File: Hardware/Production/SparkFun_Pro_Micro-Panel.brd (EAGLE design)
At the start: 104.6 x 128.3 mm, 1563 parts, among them J1 Qwiic, J13 Qwiic, J17 Qwiic, J2 Qwiic, J21 Qwiic, J25 Qwiic, J29 Qwiic, J33 Qwiic, J37 Qwiic, J41 Qwiic, J45 Qwiic, J49 Qwiic, J53 Qwiic, J57 Qwiic, J9 Qwiic, U1 3.3V, U10 3.3V, U11 ATmega32U4, U12 3.3V, U13 ATmega32U4, U14 3.3V, U15 ATmega32U4, U16 3.3V, U17 ATmega32U4, U18 3.3V, U19 ATmega32U4, U2 ATmega32U4, U20 3.3V, U21 ATmega32U4, U22 3.3V, U23 ATmega32U4, U24 3.3V, U25 ATmega32U4, U26 3.3V, U27 ATmega32U4, U28 3.3V, U29 ATmega32U4, U3 ATmega32U4, U30 3.3V, U4 3.3V, U5 ATmega32U4, U6 3.3V, U7 ATmega32U4, U8 3.3V, U9 ATmega32U4, Y1 32MHz, Y10 32MHz, Y11 32MHz, Y12 32MHz, Y13 32MHz, Y14 32MHz, Y15 32MHz, Y2 32MHz, Y3 32MHz, Y4 32MHz, Y5 32MHz, Y6 32MHz, Y7 32MHz, Y8 32MHz, Y9 32MHz

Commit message: Adding production panel, pro micro FP test brd, and castellated test lbr.
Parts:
- U$100, U$164, U$228, U$292, U$356, U$420, U$484, U$548, U$612, U$676, U$740, U$804, U$868, U$932: device buzzard_labels (18):3V39 -> buzzard_labels (15):A29
- U$101, U$165, U$229, U$293, U$357, U$421, U$485, U$549, U$613, U$677, U$741, U$805, U$869, U$933: device buzzard_labels (15):A310 -> buzzard_labels (15):A18
- U$102, U$166, U$230, U$294, U$358, U$422, U$486, U$550, U$614, U$678, U$742, U$806, U$870, U$934: device buzzard_labels (15):A29 -> buzzard_labels (15):A07
- U$103, U$167, U$231, U$295, U$359, U$423, U$487, U$551, U$615, U$679, U$743, U$807, U$871, U$935: device buzzard_labels (15):A18 -> buzzard_labels (15):156
- U$104, U$168, U$232, U$296, U$360, U$424, U$488, U$552, U$616, U$680, U$744, U$808, U$872, U$936: device buzzard_labels (15):A07 -> buzzard_labels (15):145
- U$105, U$169, U$233, U$297, U$361, U$425, U$489, U$553, U$617, U$681, U$745, U$809, U$873, U$937: device buzzard_labels (15):156 -> buzzard_labels (15):164
- U$106, U$170, U$234, U$298, U$362, U$426, U$490, U$554, U$618, U$682, U$746, U$810, U$874, U$938: device buzzard_labels (15):145 -> buzzard_labels (14):104
- U$107, U$171, U$235, U$299, U$363, U$427, U$491, U$555, U$619, U$683, U$747, U$811, U$875, U$939: device buzzard_labels (15):164 -> buzzard_labels (15):911
- U$108, U$172, U$236, U$300, U$364, U$428, U$492, U$556, U$620, U$684, U$748, U$812, U$876, U$940: device buzzard_labels (14):104 -> buzzard_labels (15):812
- U$109, U$173, U$237, U$301, U$365, U$429, U$493, U$557, U$621, U$685, U$749, U$813, U$877, U$941: device buzzard_labels (15):911 -> buzzard_labels (15):713
- U$110, U$174, U$238, U$302, U$366, U$430, U$494, U$558, U$622, U$686, U$750, U$814, U$878, U$942: device buzzard_labels (15):812 -> buzzard_labels (15):614
- U$111, U$175, U$239, U$303, U$367, U$431, U$495, U$559, U$623, U$687, U$751, U$815, U$879, U$943: device buzzard_labels (15):713 -> buzzard_labels (15):515
- U$112, U$176, U$240, U$304, U$368, U$432, U$496, U$560, U$624, U$688, U$752, U$816, U$880, U$944: device buzzard_labels (15):614 -> buzzard_labels (13):45
- U$113, U$177, U$241, U$305, U$369, U$433, U$497, U$561, U$625, U$689, U$753, U$817, U$881, U$945: device buzzard_labels (15):515 -> buzzard_labels (15):317
- U$114, U$178, U$242, U$306, U$370, U$434, U$498, U$562, U$626, U$690, U$754, U$818, U$882, U$946: device buzzard_labels (13):45 -> buzzard_labels (15):218
- U$115, U$179, U$243, U$307, U$371, U$435, U$499, U$563, U$627, U$691, U$755, U$819, U$883, U$947: device buzzard_labels (15):317 -> buzzard_labels (16):GND4
- U$116, U$180, U$244, U$308, U$372, U$436, U$500, U$564, U$628, U$692, U$756, U$820, U$884, U$948: device buzzard_labels (15):218 -> buzzard_labels (15):RX20
- U$117, U$181, U$245, U$309, U$373, U$437, U$501, U$565, U$629, U$693, U$757, U$821, U$885, U$949: device buzzard_labels (16):GND4 -> buzzard_labels (13):TX2
- U$118, U$182, U$246, U$310, U$374, U$438, U$502, U$566, U$630, U$694, U$758, U$822, U$886, U$950: device buzzard_labels (15):RX20 -> buzzard_labels (17):GND4
- U$119, U$183, U$247, U$311, U$375, U$439, U$503, U$567, U$631, U$695, U$759, U$823, U$887, U$951: device buzzard_labels (13):TX2 -> buzzard_labels (18):3V39
- U$120, U$184, U$248, U$312, U$376, U$440, U$504, U$568, U$632, U$696, U$760, U$824, U$888, U$952: device buzzard_labels (17):GND4 -> buzzard_labels (13):G1
- U$121, U$185, U$249, U$313, U$377, U$441, U$505, U$569, U$633, U$697, U$761, U$825, U$889, U$953: device buzzard_labels (18):3V39 -> buzzard_labels (13):V0
- U$122, U$186, U$250, U$314, U$378, U$442, U$506, U$570, U$634, U$698, U$762, U$826, U$890, U$954: device buzzard_labels (13):G1 -> buzzard_labels (14):D#3
- U$123, U$187, U$251, U$315, U$379, U$443, U$507, U$571, U$635, U$699, U$763, U$827, U$891, U$955: device buzzard_labels (13):V0 -> buzzard_labels (14):D#4
- U$124, U$188, U$252, U$316, U$380, U$444, U$508, U$572, U$636, U$700, U$764, U$828, U$892, U$956: device buzzard_labels (14):D#3 -> buzzard_labels (10):PWR0
- U$125, U$189, U$253, U$317, U$381, U$445, U$509, U$573, U$637, U$701, U$765, U$829, U$893, U$957: device buzzard_labels (14):D#4 -> buzzard_labels (10):5V1
- U$126, U$190, U$254, U$318, U$382, U$446, U$510, U$574, U$638, U$702, U$766, U$830, U$894, U$958: device buzzard_labels (10):PWR0 -> buzzard_labels (11):VCC1
- U$128, U$192, U$256, U$320, U$384, U$448, U$512, U$576, U$640, U$704, U$768, U$832, U$896, U$960: device buzzard_labels (11):VCC1 -> buzzard_labels (10):5V1
- U$15: device buzzard_labels (18):3V39 -> buzzard_labels (10):5V1
- U$163, U$227, U$291, U$355, U$419, U$483, U$547, U$611, U$675, U$739, U$803, U$867, U$931, U$99: device buzzard_labels (18):3V39 -> buzzard_labels (15):A310
- U$33: value (none) -> OSHW-LOGOMINI; device buzzard_labels (18):3V39 -> SparkFun-Aesthetics:OSHW-LOGO-MINI
- U$65: value OSHW-LOGOMINI -> (none); device SparkFun-Aesthetics:OSHW-LOGO-MINI -> buzzard_labels (10):5V1
- moved U$33 23.2 mm to (34.5, 31.5), flipped to the bottom, turned to 0 degrees
- moved U$65 22.9 mm to (14.7, 20.1), flipped to the top, turned to 90 degrees
- moved U$940 12.8 mm to (77.1, 74.9)
- moved U$300 12.8 mm to (77.1, 3.81)
- moved U$620 12.8 mm to (77.1, 39.4)
- moved U$684 12.8 mm to (3.94, 74.9)
- moved U$364 12.8 mm to (3.94, 39.4)
- moved U$748 12.8 mm to (22.2, 74.9)
- moved U$812 12.8 mm to (40.5, 74.9)
- moved U$108 12.8 mm to (22.2, 3.81)
- moved U$172 12.8 mm to (40.5, 3.81)
- moved U$428 12.8 mm to (22.2, 39.4)
- moved U$492 12.8 mm to (40.5, 39.4)
- moved U$876 12.8 mm to (58.8, 74.9)
- moved U$236 12.8 mm to (58.8, 3.81)
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
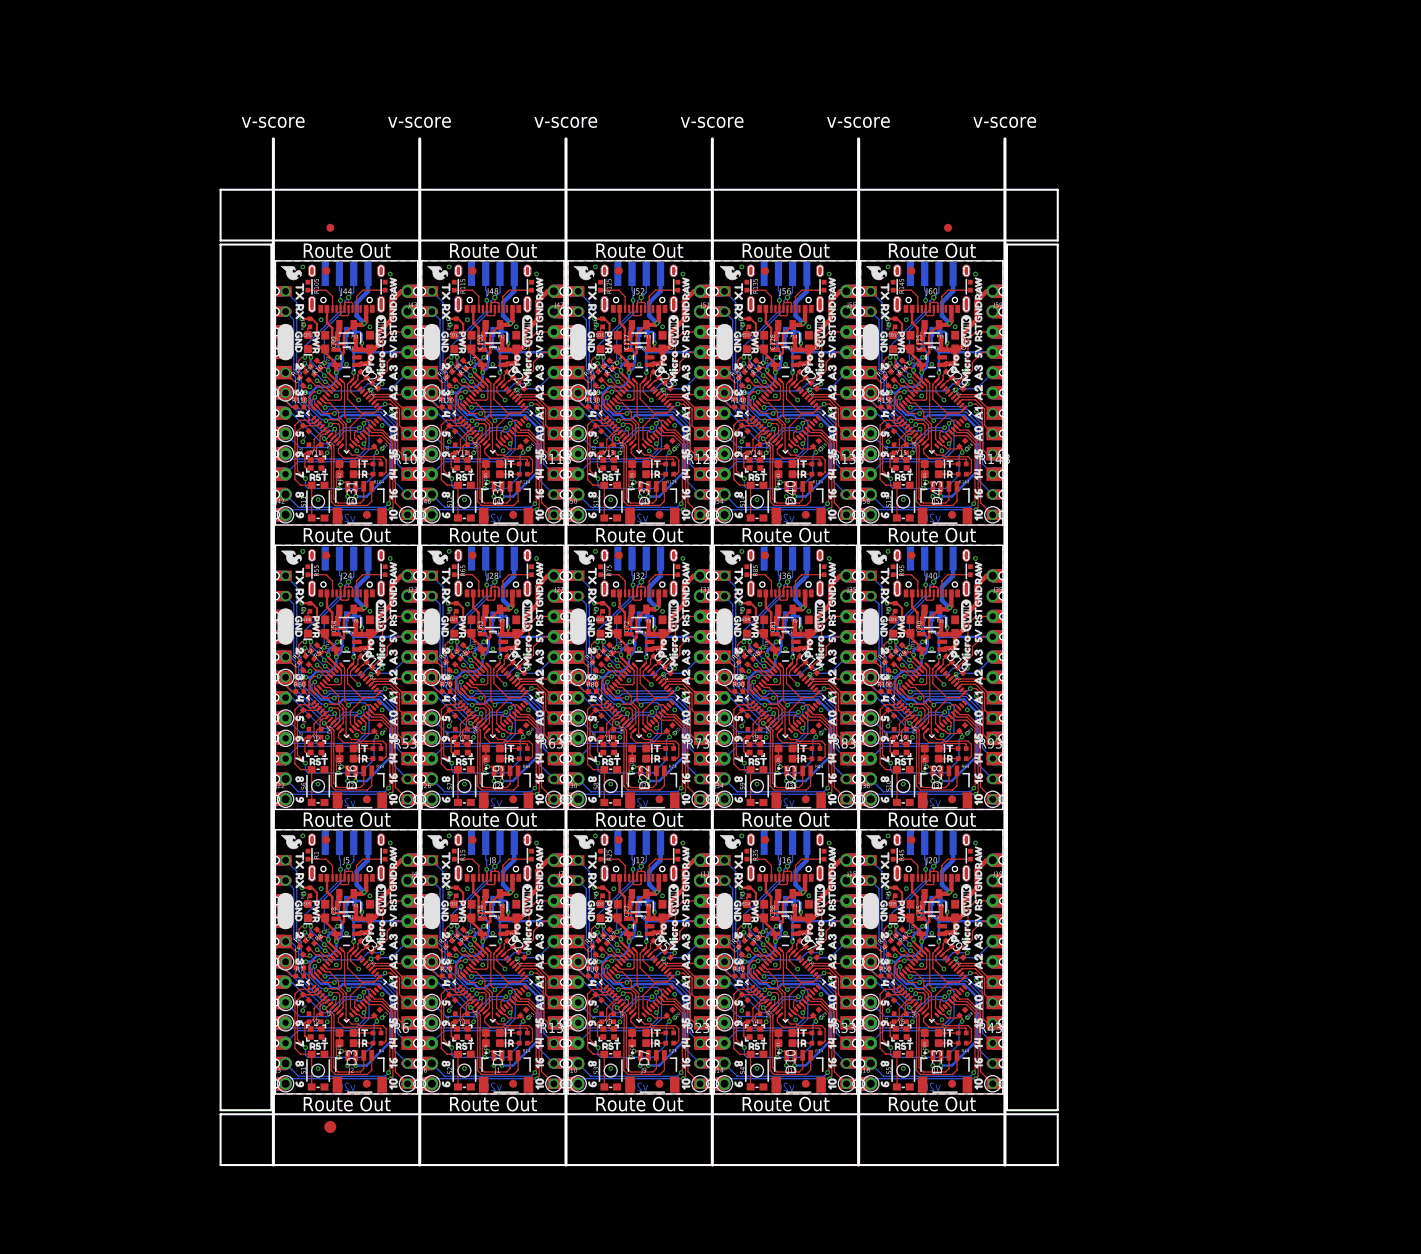
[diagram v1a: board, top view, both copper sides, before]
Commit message: Updates to Pro Micro and Frank
"Castellated" library '1x12CASTELLATED' and 'PRO_MICRO_C' footprints updated and 'PRO_MICRO_C' device updated.

Pro Micro C got uniform drill/ring sizing + added plated holes to outside in place of drills

Frank got 1U Keycap standard switch spacing and updated Pro Micro footprint.
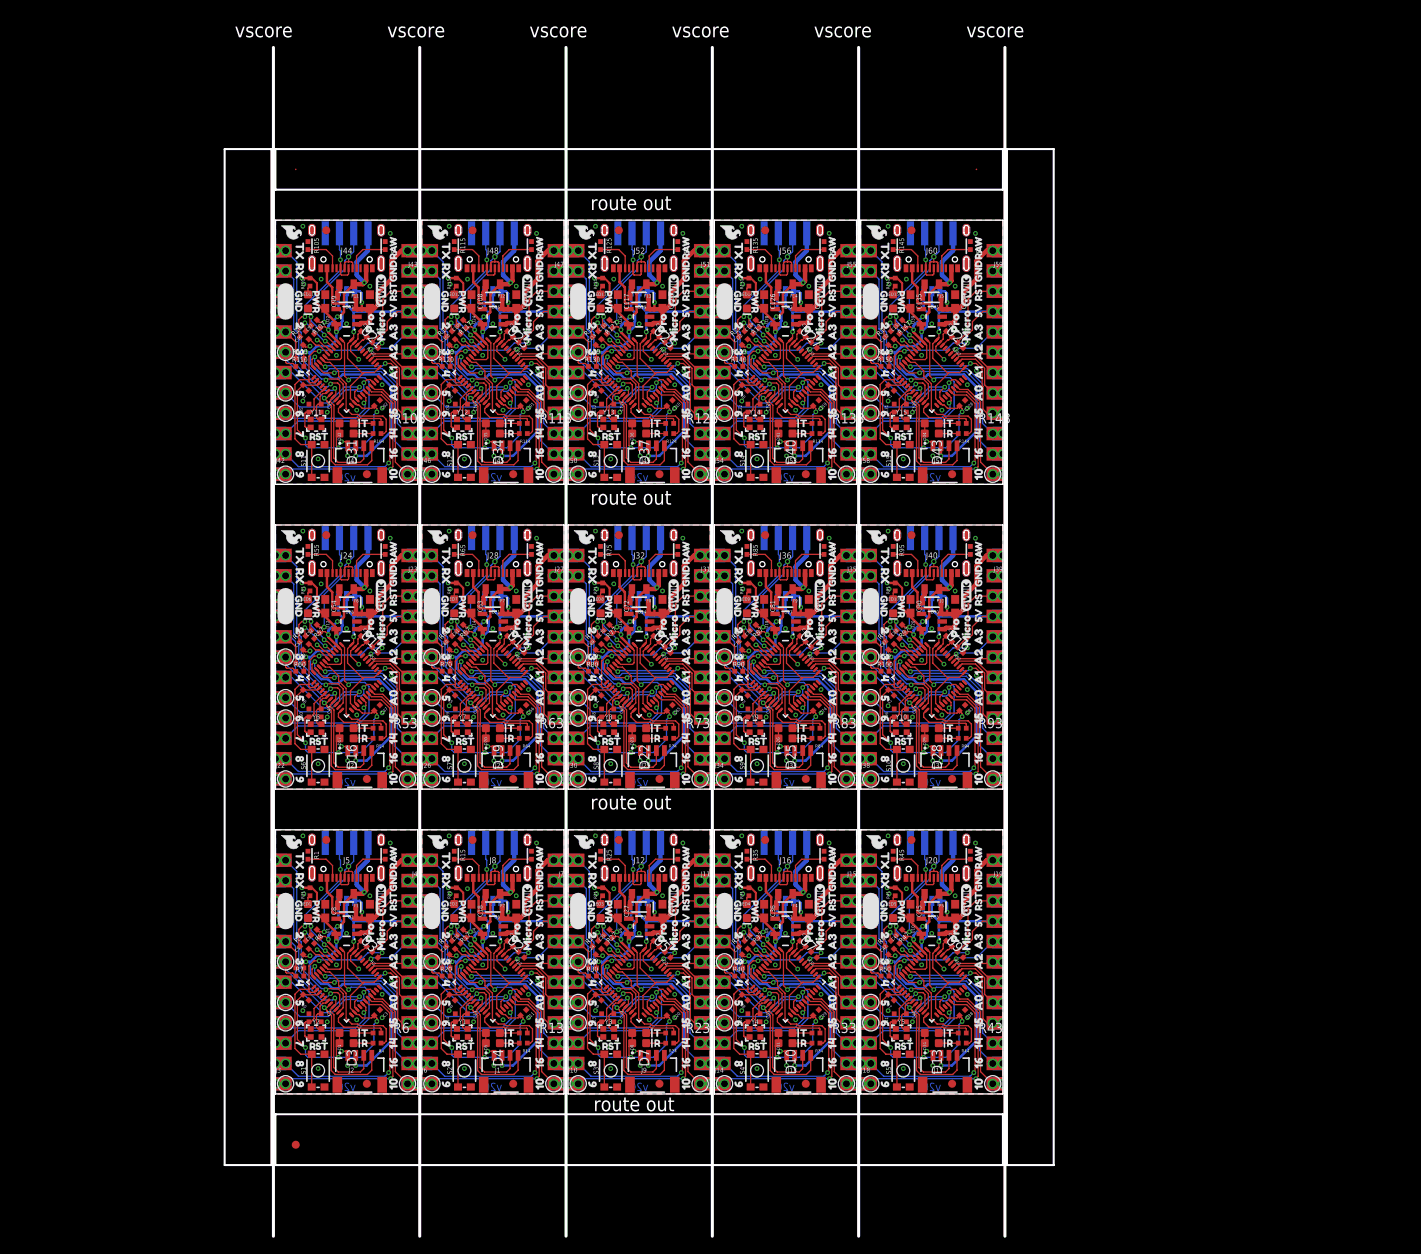
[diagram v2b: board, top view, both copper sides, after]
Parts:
- removed U$946: (no value), buzzard_labels (15):218
- removed U$947: (no value), buzzard_labels (16):GND4
- removed U$948: (no value), buzzard_labels (15):RX20
- removed U$949: (no value), buzzard_labels (13):TX2
- removed U$950: (no value), buzzard_labels (17):GND4
- removed U$951: (no value), buzzard_labels (18):3V39
- removed U$952: (no value), buzzard_labels (13):G1
- removed U$953: (no value), buzzard_labels (13):V0
- removed U$954: (no value), buzzard_labels (14):D#3
- removed U$955: (no value), buzzard_labels (14):D#4
- removed U$956: (no value), buzzard_labels (10):PWR0
- removed U$957, U$959, U$960: (no value), buzzard_labels (10):5V1
- removed U$958: (no value), buzzard_labels (11):VCC1
- E$2: device SparkFun-Aesthetics:FIDUCIAL-1X2 -> SparkFun-Aesthetics:FIDUCIAL-0.2MM
- E$3: device SparkFun-Retired:FIDUCIAL-1.5X3 -> SparkFun-Aesthetics:FIDUCIAL-0.2MM
- U$100: device buzzard_labels (15):A29 -> buzzard_labels (15):A07
- U$101: device buzzard_labels (15):A18 -> buzzard_labels (15):156
- U$102, U$401: device buzzard_labels (15):A07 -> buzzard_labels (15):145
- U$103: device buzzard_labels (15):156 -> buzzard_labels (15):164
- U$104: device buzzard_labels (15):145 -> buzzard_labels (14):104
- U$105, U$393: device buzzard_labels (15):164 -> buzzard_labels (15):911
- U$106, U$581: device buzzard_labels (14):104 -> buzzard_labels (15):812
- U$107: device buzzard_labels (15):911 -> buzzard_labels (15):713
- U$108: device buzzard_labels (15):812 -> buzzard_labels (15):614
- U$109: device buzzard_labels (15):713 -> buzzard_labels (15):515
- U$110: device buzzard_labels (15):614 -> buzzard_labels (13):45
- U$111: device buzzard_labels (15):515 -> buzzard_labels (15):317
- U$112, U$450: device buzzard_labels (13):45 -> buzzard_labels (15):218
- U$113, U$651: device buzzard_labels (15):317 -> buzzard_labels (16):GND4
- U$114, U$650: device buzzard_labels (15):218 -> buzzard_labels (15):RX20
- U$115: device buzzard_labels (16):GND4 -> buzzard_labels (13):TX2
- U$116, U$469: device buzzard_labels (15):RX20 -> buzzard_labels (17):GND4
- U$117: device buzzard_labels (13):TX2 -> buzzard_labels (18):3V39
- U$118: device buzzard_labels (17):GND4 -> buzzard_labels (13):G1
- U$119: device buzzard_labels (18):3V39 -> buzzard_labels (13):V0
- U$120: device buzzard_labels (13):G1 -> buzzard_labels (14):D#3
- U$121: device buzzard_labels (13):V0 -> buzzard_labels (14):D#4
- U$122: device buzzard_labels (14):D#3 -> buzzard_labels (10):PWR0
- U$123, U$251, U$315: device buzzard_labels (14):D#4 -> buzzard_labels (10):5V1
- U$124: device buzzard_labels (10):PWR0 -> buzzard_labels (11):VCC1
- U$126: device buzzard_labels (11):VCC1 -> buzzard_labels (10):5V1
- U$127, U$253: value (none) -> OSHW-LOGOMINI; device buzzard_labels (10):5V1 -> SparkFun-Aesthetics:OSHW-LOGO-MINI
- U$128, U$191, U$317: device buzzard_labels (10):5V1 -> buzzard_labels (13):45
- U$129: value OSHW-LOGOMINI -> (none); device SparkFun-Aesthetics:OSHW-LOGO-MINI -> buzzard_labels (13):TX2
- U$130: device buzzard_labels (13):45 -> buzzard_labels (14):104
- U$131: device buzzard_labels (13):TX2 -> buzzard_labels (14):MICRO1
- U$132: device SparkFun-Aesthetics:PRODUCTION_INSTRUCTIONS -> buzzard_labels (14):PRO0
- U$133: device buzzard_labels (14):104 -> buzzard_labels (15):156
- U$134: device buzzard_labels (14):MICRO1 -> buzzard_labels (15):164
- U$135: device buzzard_labels (14):PRO0 -> buzzard_labels (15):218
- U$136, U$615: device buzzard_labels (15):156 -> buzzard_labels (15):317
- U$137, U$361: device buzzard_labels (15):164 -> buzzard_labels (15):515
- U$138: device buzzard_labels (15):218 -> buzzard_labels (15):614
- U$139: device buzzard_labels (15):317 -> buzzard_labels (15):713
- U$140: device buzzard_labels (15):515 -> buzzard_labels (15):812
- U$141: device buzzard_labels (15):614 -> buzzard_labels (15):911
- U$142: device buzzard_labels (15):713 -> buzzard_labels (15):A07
- U$143: device buzzard_labels (15):812 -> buzzard_labels (15):A18
- U$144: device buzzard_labels (15):911 -> buzzard_labels (15):A29
- U$145: device buzzard_labels (15):A07 -> buzzard_labels (15):A310
- U$146, U$933: device buzzard_labels (15):A18 -> buzzard_labels (15):RX20
- U$147, U$932: device buzzard_labels (15):A29 -> buzzard_labels (16):GND4
- U$148: device buzzard_labels (15):A310 -> buzzard_labels (16):RST3
- U$149: device buzzard_labels (15):RX20 -> buzzard_labels (15):145
- U$150: device buzzard_labels (16):GND4 -> buzzard_labels (17):R9
- U$151, U$599: device buzzard_labels (16):RST3 -> buzzard_labels (17):RAW5
- U$152: device buzzard_labels (15):145 -> buzzard_labels (17):T8
- U$153, U$537: device buzzard_labels (17):R9 -> buzzard_labels (17):RST3
- U$154: device buzzard_labels (17):RAW5 -> buzzard_labels (17):GND4
- U$155: device buzzard_labels (17):T8 -> buzzard_labels (18):C5
- U$156: device buzzard_labels (17):RST3 -> buzzard_labels (18):MICRO4
- U$157: device buzzard_labels (17):GND4 -> buzzard_labels (18):PRO3
- U$158: device buzzard_labels (18):C5 -> buzzard_labels (17):RAW5
- U$159: device buzzard_labels (18):MICRO4 -> buzzard_labels (17):RST3
- U$160: device buzzard_labels (18):PRO3 -> buzzard_labels (15):A310
- U$161, U$602: device buzzard_labels (17):RAW5 -> buzzard_labels (15):A29
- U$162, U$540: device buzzard_labels (17):RST3 -> buzzard_labels (15):A18
- U$163: device buzzard_labels (15):A310 -> buzzard_labels (15):A07
- U$164: device buzzard_labels (15):A29 -> buzzard_labels (15):156
- U$165, U$338: device buzzard_labels (15):A18 -> buzzard_labels (15):145
- U$166: device buzzard_labels (15):A07 -> buzzard_labels (15):164
- U$167: device buzzard_labels (15):156 -> buzzard_labels (14):104
- U$168: device buzzard_labels (15):145 -> buzzard_labels (15):911
- U$169, U$329: device buzzard_labels (15):164 -> buzzard_labels (15):812
- U$170, U$517: device buzzard_labels (14):104 -> buzzard_labels (15):713
- U$171: device buzzard_labels (15):911 -> buzzard_labels (15):614
- U$172: device buzzard_labels (15):812 -> buzzard_labels (15):515
- U$173: device buzzard_labels (15):713 -> buzzard_labels (13):45
- U$174: device buzzard_labels (15):614 -> buzzard_labels (15):317
- U$175: device buzzard_labels (15):515 -> buzzard_labels (15):218
- U$176: device buzzard_labels (13):45 -> buzzard_labels (16):GND4
- U$177, U$587: device buzzard_labels (15):317 -> buzzard_labels (15):RX20
- U$178: device buzzard_labels (15):218 -> buzzard_labels (13):TX2
- U$179, U$406: device buzzard_labels (16):GND4 -> buzzard_labels (17):GND4
- U$180: device buzzard_labels (15):RX20 -> buzzard_labels (18):3V39
- U$181: device buzzard_labels (13):TX2 -> buzzard_labels (13):G1
- U$182: device buzzard_labels (17):GND4 -> buzzard_labels (13):V0
- U$183: device buzzard_labels (18):3V39 -> buzzard_labels (14):D#3
- U$184: device buzzard_labels (13):G1 -> buzzard_labels (14):D#4
- U$185: device buzzard_labels (13):V0 -> buzzard_labels (10):PWR0
- U$186, U$314, U$378: device buzzard_labels (14):D#3 -> buzzard_labels (10):5V1
- U$187: device buzzard_labels (14):D#4 -> buzzard_labels (11):VCC1
- U$188, U$252: device buzzard_labels (10):PWR0 -> buzzard_labels (10):5V1
- U$190: value (none) -> OSHW-LOGOMINI; device buzzard_labels (11):VCC1 -> SparkFun-Aesthetics:OSHW-LOGO-MINI
- U$192, U$255, U$381: device buzzard_labels (10):5V1 -> buzzard_labels (13):TX2
- U$193: value OSHW-LOGOMINI -> (none); device SparkFun-Aesthetics:OSHW-LOGO-MINI -> buzzard_labels (14):104
- U$194: device buzzard_labels (13):45 -> buzzard_labels (14):MICRO1
- U$195: device buzzard_labels (13):TX2 -> buzzard_labels (14):PRO0
- U$196: device SparkFun-Aesthetics:PRODUCTION_INSTRUCTIONS -> buzzard_labels (15):156
- U$197: device buzzard_labels (14):104 -> buzzard_labels (15):164
- U$198: device buzzard_labels (14):MICRO1 -> buzzard_labels (15):218
- U$199: device buzzard_labels (14):PRO0 -> buzzard_labels (15):317
- U$20: value (none) -> OSHW-LOGOMINI; device SparkFun-Aesthetics:PRODUCTION_INSTRUCTIONS -> SparkFun-Aesthetics:OSHW-LOGO-MINI
- U$200, U$487: device buzzard_labels (15):156 -> buzzard_labels (15):515
- U$201, U$297: device buzzard_labels (15):164 -> buzzard_labels (15):614
- U$202: device buzzard_labels (15):218 -> buzzard_labels (15):713
- U$203: device buzzard_labels (15):317 -> buzzard_labels (15):812
- U$204: device buzzard_labels (15):515 -> buzzard_labels (15):911
- U$205: device buzzard_labels (15):614 -> buzzard_labels (15):A07
- U$206: device buzzard_labels (15):713 -> buzzard_labels (15):A18
- U$207: device buzzard_labels (15):812 -> buzzard_labels (15):A29
- U$208: device buzzard_labels (15):911 -> buzzard_labels (15):A310
- U$209, U$870: device buzzard_labels (15):A07 -> buzzard_labels (15):RX20
- U$210, U$869: device buzzard_labels (15):A18 -> buzzard_labels (16):GND4
- U$211: device buzzard_labels (15):A29 -> buzzard_labels (16):RST3
- U$212, U$291: device buzzard_labels (15):A310 -> buzzard_labels (15):145
- U$213: device buzzard_labels (15):RX20 -> buzzard_labels (17):R9
- U$214, U$662: device buzzard_labels (16):GND4 -> buzzard_labels (17):RAW5
- U$215: device buzzard_labels (16):RST3 -> buzzard_labels (17):T8
- U$216, U$600: device buzzard_labels (15):145 -> buzzard_labels (17):RST3
- U$217: device buzzard_labels (17):R9 -> buzzard_labels (17):GND4
- U$218: device buzzard_labels (17):RAW5 -> buzzard_labels (18):C5
- U$219: device buzzard_labels (17):T8 -> buzzard_labels (18):MICRO4
- U$220: device buzzard_labels (17):RST3 -> buzzard_labels (18):PRO3
- U$221: device buzzard_labels (17):GND4 -> buzzard_labels (17):RAW5
- U$222: device buzzard_labels (18):C5 -> buzzard_labels (17):RST3
- U$223: device buzzard_labels (18):MICRO4 -> buzzard_labels (15):A310
- U$224: device buzzard_labels (18):PRO3 -> buzzard_labels (15):A29
- U$225, U$666: device buzzard_labels (17):RAW5 -> buzzard_labels (15):A18
- U$226, U$604: device buzzard_labels (17):RST3 -> buzzard_labels (15):A07
- U$227: device buzzard_labels (15):A310 -> buzzard_labels (15):156
- U$228, U$275: device buzzard_labels (15):A29 -> buzzard_labels (15):145
- U$229: device buzzard_labels (15):A18 -> buzzard_labels (15):164
- U$230: device buzzard_labels (15):A07 -> buzzard_labels (14):104
- U$231, U$456: device buzzard_labels (15):156 -> buzzard_labels (15):911
- U$232: device buzzard_labels (15):145 -> buzzard_labels (15):812
- U$233, U$265: device buzzard_labels (15):164 -> buzzard_labels (15):713
- U$234, U$453: device buzzard_labels (14):104 -> buzzard_labels (15):614
- U$235: device buzzard_labels (15):911 -> buzzard_labels (15):515
- U$236: device buzzard_labels (15):812 -> buzzard_labels (13):45
- U$237: device buzzard_labels (15):713 -> buzzard_labels (15):317
- U$238: device buzzard_labels (15):614 -> buzzard_labels (15):218
- U$239, U$588: device buzzard_labels (15):515 -> buzzard_labels (16):GND4
- U$240: device buzzard_labels (13):45 -> buzzard_labels (15):RX20
- U$241: device buzzard_labels (15):317 -> buzzard_labels (13):TX2
- U$242: device buzzard_labels (15):218 -> buzzard_labels (17):GND4
- U$243: device buzzard_labels (16):GND4 -> buzzard_labels (18):3V39
- U$244: device buzzard_labels (15):RX20 -> buzzard_labels (13):G1
- U$245: device buzzard_labels (13):TX2 -> buzzard_labels (13):V0
- U$246: device buzzard_labels (17):GND4 -> buzzard_labels (14):D#3
- U$247: device buzzard_labels (18):3V39 -> buzzard_labels (14):D#4
- U$248: device buzzard_labels (13):G1 -> buzzard_labels (10):PWR0
- U$249, U$377, U$441: device buzzard_labels (13):V0 -> buzzard_labels (10):5V1
- U$250: device buzzard_labels (14):D#3 -> buzzard_labels (11):VCC1
- U$254: device buzzard_labels (11):VCC1 -> buzzard_labels (13):45
- U$256, U$319, U$445: device buzzard_labels (10):5V1 -> buzzard_labels (14):104
- U$257: value OSHW-LOGOMINI -> (none); device SparkFun-Aesthetics:OSHW-LOGO-MINI -> buzzard_labels (14):MICRO1
- U$258: device buzzard_labels (13):45 -> buzzard_labels (14):PRO0
- U$259: device buzzard_labels (13):TX2 -> buzzard_labels (15):156
- U$260: device SparkFun-Aesthetics:PRODUCTION_INSTRUCTIONS -> buzzard_labels (15):164
- U$261, U$490: device buzzard_labels (14):104 -> buzzard_labels (15):218
- U$262: device buzzard_labels (14):MICRO1 -> buzzard_labels (15):317
- U$263: device buzzard_labels (14):PRO0 -> buzzard_labels (15):515
- U$264, U$423: device buzzard_labels (15):156 -> buzzard_labels (15):614
- U$266: device buzzard_labels (15):218 -> buzzard_labels (15):812
- U$267: device buzzard_labels (15):317 -> buzzard_labels (15):911
- U$268: device buzzard_labels (15):515 -> buzzard_labels (15):A07
- U$269: device buzzard_labels (15):614 -> buzzard_labels (15):A18
- U$270: device buzzard_labels (15):713 -> buzzard_labels (15):A29
- U$271: device buzzard_labels (15):812 -> buzzard_labels (15):A310
- U$272, U$555: device buzzard_labels (15):911 -> buzzard_labels (15):RX20
- U$273, U$806: device buzzard_labels (15):A07 -> buzzard_labels (16):GND4
- U$274: device buzzard_labels (15):A18 -> buzzard_labels (16):RST3
- U$276: device buzzard_labels (15):A310 -> buzzard_labels (17):R9
- U$277, U$725: device buzzard_labels (15):RX20 -> buzzard_labels (17):RAW5
- U$278: device buzzard_labels (16):GND4 -> buzzard_labels (17):T8
- U$279, U$663: device buzzard_labels (16):RST3 -> buzzard_labels (17):RST3
- U$280, U$872: device buzzard_labels (15):145 -> buzzard_labels (17):GND4
- U$281: device buzzard_labels (17):R9 -> buzzard_labels (18):C5
- U$282: device buzzard_labels (17):RAW5 -> buzzard_labels (18):MICRO4
- U$283: device buzzard_labels (17):T8 -> buzzard_labels (18):PRO3
- U$284: device buzzard_labels (17):RST3 -> buzzard_labels (17):RAW5
- U$285: device buzzard_labels (17):GND4 -> buzzard_labels (17):RST3
- U$286: device buzzard_labels (18):C5 -> buzzard_labels (15):A310
- U$287: device buzzard_labels (18):MICRO4 -> buzzard_labels (15):A29
- U$288: device buzzard_labels (18):PRO3 -> buzzard_labels (15):A18
- U$289, U$730: device buzzard_labels (17):RAW5 -> buzzard_labels (15):A07
- U$290, U$668: device buzzard_labels (17):RST3 -> buzzard_labels (15):156
- U$292: device buzzard_labels (15):A29 -> buzzard_labels (15):164
- U$293: device buzzard_labels (15):A18 -> buzzard_labels (14):104
- U$294: device buzzard_labels (15):A07 -> buzzard_labels (15):911
- U$295, U$392: device buzzard_labels (15):156 -> buzzard_labels (15):812
- U$296: device buzzard_labels (15):145 -> buzzard_labels (15):713
- U$298, U$389: device buzzard_labels (14):104 -> buzzard_labels (15):515
- U$299: device buzzard_labels (15):911 -> buzzard_labels (13):45
- U$300: device buzzard_labels (15):812 -> buzzard_labels (15):317
- U$301: device buzzard_labels (15):713 -> buzzard_labels (15):218
- U$302, U$525: device buzzard_labels (15):614 -> buzzard_labels (16):GND4
- U$303, U$524: device buzzard_labels (15):515 -> buzzard_labels (15):RX20
- U$304, U$66: device buzzard_labels (13):45 -> buzzard_labels (13):TX2
- U$305: device buzzard_labels (15):317 -> buzzard_labels (17):GND4
- U$306: device buzzard_labels (15):218 -> buzzard_labels (18):3V39
- U$307: device buzzard_labels (16):GND4 -> buzzard_labels (13):G1
- U$308: device buzzard_labels (15):RX20 -> buzzard_labels (13):V0
- U$309: device buzzard_labels (13):TX2 -> buzzard_labels (14):D#3
- U$310: device buzzard_labels (17):GND4 -> buzzard_labels (14):D#4
- U$311: device buzzard_labels (18):3V39 -> buzzard_labels (10):PWR0
- U$312, U$440, U$504: device buzzard_labels (13):G1 -> buzzard_labels (10):5V1
- U$313: device buzzard_labels (13):V0 -> buzzard_labels (11):VCC1
- U$316: value (none) -> OSHW-LOGOMINI; device buzzard_labels (10):PWR0 -> SparkFun-Aesthetics:OSHW-LOGO-MINI
- U$318: device buzzard_labels (11):VCC1 -> buzzard_labels (13):TX2
- U$320, U$383, U$509: device buzzard_labels (10):5V1 -> buzzard_labels (14):MICRO1
- U$321: value OSHW-LOGOMINI -> (none); device SparkFun-Aesthetics:OSHW-LOGO-MINI -> buzzard_labels (14):PRO0
- U$322: device buzzard_labels (13):45 -> buzzard_labels (15):156
- U$323: device buzzard_labels (13):TX2 -> buzzard_labels (15):164
- U$324: device SparkFun-Aesthetics:PRODUCTION_INSTRUCTIONS -> buzzard_labels (15):218
- U$325, U$426: device buzzard_labels (14):104 -> buzzard_labels (15):317
- U$326: device buzzard_labels (14):MICRO1 -> buzzard_labels (15):515
- U$327: device buzzard_labels (14):PRO0 -> buzzard_labels (15):614
- U$328, U$359: device buzzard_labels (15):156 -> buzzard_labels (15):713
- U$33: value OSHW-LOGOMINI -> (none); device SparkFun-Aesthetics:OSHW-LOGO-MINI -> buzzard_labels (13):45
- U$330: device buzzard_labels (15):218 -> buzzard_labels (15):911
- U$331: device buzzard_labels (15):317 -> buzzard_labels (15):A07
- U$332: device buzzard_labels (15):515 -> buzzard_labels (15):A18
- U$333: device buzzard_labels (15):614 -> buzzard_labels (15):A29
- U$334: device buzzard_labels (15):713 -> buzzard_labels (15):A310
- U$335, U$492: device buzzard_labels (15):812 -> buzzard_labels (15):RX20
- U$336, U$491: device buzzard_labels (15):911 -> buzzard_labels (16):GND4
- U$337: device buzzard_labels (15):A07 -> buzzard_labels (16):RST3
- U$339: device buzzard_labels (15):A29 -> buzzard_labels (17):R9
- U$340, U$788: device buzzard_labels (15):A310 -> buzzard_labels (17):RAW5
- U$341: device buzzard_labels (15):RX20 -> buzzard_labels (17):T8
- U$342, U$726: device buzzard_labels (16):GND4 -> buzzard_labels (17):RST3
- U$343: device buzzard_labels (16):RST3 -> buzzard_labels (17):GND4
- U$344: device buzzard_labels (15):145 -> buzzard_labels (18):C5
- U$345: device buzzard_labels (17):R9 -> buzzard_labels (18):MICRO4
- U$346: device buzzard_labels (17):RAW5 -> buzzard_labels (18):PRO3
- U$347: device buzzard_labels (17):T8 -> buzzard_labels (17):RAW5
- U$349: device buzzard_labels (17):GND4 -> buzzard_labels (15):A310
- U$350: device buzzard_labels (18):C5 -> buzzard_labels (15):A29
- U$351: device buzzard_labels (18):MICRO4 -> buzzard_labels (15):A18
- U$352: device buzzard_labels (18):PRO3 -> buzzard_labels (15):A07
- U$353, U$794: device buzzard_labels (17):RAW5 -> buzzard_labels (15):156
- U$354, U$732: device buzzard_labels (17):RST3 -> buzzard_labels (15):145
- U$355: device buzzard_labels (15):A310 -> buzzard_labels (15):164
- U$356: device buzzard_labels (15):A29 -> buzzard_labels (14):104
- U$357: device buzzard_labels (15):A18 -> buzzard_labels (15):911
- U$358: device buzzard_labels (15):A07 -> buzzard_labels (15):812
- U$360: device buzzard_labels (15):145 -> buzzard_labels (15):614
- U$362: device buzzard_labels (14):104 -> buzzard_labels (13):45
- U$363: device buzzard_labels (15):911 -> buzzard_labels (15):317
- U$364: device buzzard_labels (15):812 -> buzzard_labels (15):218
- U$365, U$462: device buzzard_labels (15):713 -> buzzard_labels (16):GND4
- U$366, U$461: device buzzard_labels (15):614 -> buzzard_labels (15):RX20
- U$367: device buzzard_labels (15):515 -> buzzard_labels (13):TX2
- U$368: device buzzard_labels (13):45 -> buzzard_labels (17):GND4
- U$369: device buzzard_labels (15):317 -> buzzard_labels (18):3V39
- U$370: device buzzard_labels (15):218 -> buzzard_labels (13):G1
- U$371: device buzzard_labels (16):GND4 -> buzzard_labels (13):V0
- U$372: device buzzard_labels (15):RX20 -> buzzard_labels (14):D#3
- U$373: device buzzard_labels (13):TX2 -> buzzard_labels (14):D#4
- U$374: device buzzard_labels (17):GND4 -> buzzard_labels (10):PWR0
- U$375, U$503, U$567: device buzzard_labels (18):3V39 -> buzzard_labels (10):5V1
- U$376: device buzzard_labels (13):G1 -> buzzard_labels (11):VCC1
- U$379: value (none) -> OSHW-LOGOMINI; device buzzard_labels (14):D#4 -> SparkFun-Aesthetics:OSHW-LOGO-MINI
- U$380: device buzzard_labels (10):PWR0 -> buzzard_labels (13):45
- U$382: device buzzard_labels (11):VCC1 -> buzzard_labels (14):104
- U$384, U$447, U$573: device buzzard_labels (10):5V1 -> buzzard_labels (14):PRO0
- U$385: value OSHW-LOGOMINI -> (none); device SparkFun-Aesthetics:OSHW-LOGO-MINI -> buzzard_labels (15):156
- U$386: device buzzard_labels (13):45 -> buzzard_labels (15):164
- U$387: device buzzard_labels (13):TX2 -> buzzard_labels (15):218
- U$388: device SparkFun-Aesthetics:PRODUCTION_INSTRUCTIONS -> buzzard_labels (15):317
- U$390: device buzzard_labels (14):MICRO1 -> buzzard_labels (15):614
- U$391: device buzzard_labels (14):PRO0 -> buzzard_labels (15):713
- U$394: device buzzard_labels (15):218 -> buzzard_labels (15):A07
- U$395: device buzzard_labels (15):317 -> buzzard_labels (15):A18
- U$396: device buzzard_labels (15):515 -> buzzard_labels (15):A29
- U$397: device buzzard_labels (15):614 -> buzzard_labels (15):A310
- U$398, U$429: device buzzard_labels (15):713 -> buzzard_labels (15):RX20
- U$399, U$428: device buzzard_labels (15):812 -> buzzard_labels (16):GND4
- U$400: device buzzard_labels (15):911 -> buzzard_labels (16):RST3
- U$402: device buzzard_labels (15):A18 -> buzzard_labels (17):R9
- U$403, U$851: device buzzard_labels (15):A29 -> buzzard_labels (17):RAW5
- U$404: device buzzard_labels (15):A310 -> buzzard_labels (17):T8
- U$405, U$789: device buzzard_labels (15):RX20 -> buzzard_labels (17):RST3
- U$407: device buzzard_labels (16):RST3 -> buzzard_labels (18):C5
- U$408: device buzzard_labels (15):145 -> buzzard_labels (18):MICRO4
- U$409: device buzzard_labels (17):R9 -> buzzard_labels (18):PRO3
- U$411: device buzzard_labels (17):T8 -> buzzard_labels (17):RST3
- U$412: device buzzard_labels (17):RST3 -> buzzard_labels (15):A310
- U$413: device buzzard_labels (17):GND4 -> buzzard_labels (15):A29
- U$414: device buzzard_labels (18):C5 -> buzzard_labels (15):A18
- U$415: device buzzard_labels (18):MICRO4 -> buzzard_labels (15):A07
- U$416: device buzzard_labels (18):PRO3 -> buzzard_labels (15):156
- U$417, U$858: device buzzard_labels (17):RAW5 -> buzzard_labels (15):145
- U$418, U$796: device buzzard_labels (17):RST3 -> buzzard_labels (15):164
- U$419: device buzzard_labels (15):A310 -> buzzard_labels (14):104
- U$420: device buzzard_labels (15):A29 -> buzzard_labels (15):911
- U$421: device buzzard_labels (15):A18 -> buzzard_labels (15):812
- U$422: device buzzard_labels (15):A07 -> buzzard_labels (15):713
- U$424: device buzzard_labels (15):145 -> buzzard_labels (15):515
- U$425: device buzzard_labels (15):164 -> buzzard_labels (13):45
- U$427: device buzzard_labels (15):911 -> buzzard_labels (15):218
- U$430: device buzzard_labels (15):614 -> buzzard_labels (13):TX2
- U$431: device buzzard_labels (15):515 -> buzzard_labels (17):GND4
- U$432: device buzzard_labels (13):45 -> buzzard_labels (18):3V39
- U$433: device buzzard_labels (15):317 -> buzzard_labels (13):G1
- U$434: device buzzard_labels (15):218 -> buzzard_labels (13):V0
- U$435: device buzzard_labels (16):GND4 -> buzzard_labels (14):D#3
- U$436: device buzzard_labels (15):RX20 -> buzzard_labels (14):D#4
- U$437: device buzzard_labels (13):TX2 -> buzzard_labels (10):PWR0
- U$438, U$566, U$630: device buzzard_labels (17):GND4 -> buzzard_labels (10):5V1
- U$439: device buzzard_labels (18):3V39 -> buzzard_labels (11):VCC1
- U$442: value (none) -> OSHW-LOGOMINI; device buzzard_labels (14):D#3 -> SparkFun-Aesthetics:OSHW-LOGO-MINI
- U$443: device buzzard_labels (14):D#4 -> buzzard_labels (13):45
- U$444: device buzzard_labels (10):PWR0 -> buzzard_labels (13):TX2
- U$446: device buzzard_labels (11):VCC1 -> buzzard_labels (14):MICRO1
- U$448, U$511, U$637: device buzzard_labels (10):5V1 -> buzzard_labels (15):156
- U$449: value OSHW-LOGOMINI -> (none); device SparkFun-Aesthetics:OSHW-LOGO-MINI -> buzzard_labels (15):164
- U$451: device buzzard_labels (13):TX2 -> buzzard_labels (15):317
- U$452: device SparkFun-Aesthetics:PRODUCTION_INSTRUCTIONS -> buzzard_labels (15):515
- U$454: device buzzard_labels (14):MICRO1 -> buzzard_labels (15):713
- U$455: device buzzard_labels (14):PRO0 -> buzzard_labels (15):812
- U$457: device buzzard_labels (15):164 -> buzzard_labels (15):A07
- U$458: device buzzard_labels (15):218 -> buzzard_labels (15):A18
- U$459: device buzzard_labels (15):317 -> buzzard_labels (15):A29
- U$460: device buzzard_labels (15):515 -> buzzard_labels (15):A310
- U$463: device buzzard_labels (15):812 -> buzzard_labels (16):RST3
- U$464: device buzzard_labels (15):911 -> buzzard_labels (15):145
- U$465: device buzzard_labels (15):A07 -> buzzard_labels (17):R9
- U$466, U$914: device buzzard_labels (15):A18 -> buzzard_labels (17):RAW5
- U$467: device buzzard_labels (15):A29 -> buzzard_labels (17):T8
- U$468, U$852: device buzzard_labels (15):A310 -> buzzard_labels (17):RST3
- U$470: device buzzard_labels (16):GND4 -> buzzard_labels (18):C5
- U$471: device buzzard_labels (16):RST3 -> buzzard_labels (18):MICRO4
- U$472: device buzzard_labels (15):145 -> buzzard_labels (18):PRO3
- U$473: device buzzard_labels (17):R9 -> buzzard_labels (17):RAW5
- U$474, U$90: device buzzard_labels (17):RAW5 -> buzzard_labels (17):RST3
- U$475: device buzzard_labels (17):T8 -> buzzard_labels (15):A310
- U$476, U$98: device buzzard_labels (17):RST3 -> buzzard_labels (15):A29
- U$477: device buzzard_labels (17):GND4 -> buzzard_labels (15):A18
- U$478: device buzzard_labels (18):C5 -> buzzard_labels (15):A07
- U$479: device buzzard_labels (18):MICRO4 -> buzzard_labels (15):156
- U$480: device buzzard_labels (18):PRO3 -> buzzard_labels (15):145
- U$481, U$922: device buzzard_labels (17):RAW5 -> buzzard_labels (15):164
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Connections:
- removed net 3.3V12: C117.2, J49.2, JP52.1, R121.2, R129.2, R130.2, U26.5
- removed net 3.3V13: C126.2, J53.2, JP56.1, R131.2, R139.2, R140.2, U28.5
- removed net 3.3V14: C135.2, J57.2, JP60.1, R141.2, R149.2, R150.2, U30.5
- removed net 3.3V2: C27.2, J9.2, JP11.1, R21.2, R29.2, R30.2, U6.5
- removed net 3.3V3: C36.2, J13.2, JP16.1, R31.2, R39.2, R40.2, U8.5
- removed net 3.3V4: C45.2, J17.2, JP20.1, R41.2, R49.2, R50.2, U10.5
- removed net 3.3V7: C72.2, J29.2, JP32.1, R71.2, R79.2, R80.2, U16.5
- removed net 3.3V8: C81.2, J33.2, JP36.1, R81.2, R89.2, R90.2, U18.5
- removed net 3.3V9: C90.2, J37.2, JP40.1, R100.2, R91.2, R99.2, U20.5
- removed net A10: J11.7, U5.37
- removed net A11: J11.8, U5.36
- removed net A12: J15.5, U7.39
- removed net A13: J15.6, U7.38
- removed net A14: J15.7, U7.37
- removed net A15: J15.8, U7.36
- removed net A16: J19.5, U9.39
- removed net A17: J19.6, U9.38
- removed net A18: J19.7, U9.37
- removed net A19: J19.8, U9.36
- removed net A28: J31.5, U15.39
- removed net A29: J31.6, U15.38
- removed net A30: J31.7, U15.37
- removed net A31: J31.8, U15.36
- removed net A32: J35.5, U17.39
- removed net A33: J35.6, U17.38
- removed net A34: J35.7, U17.37
- removed net A35: J35.8, U17.36
- removed net A36: J39.5, U19.39
- removed net A37: J39.6, U19.38
- removed net A38: J39.7, U19.37
- removed net A39: J39.8, U19.36
- removed net A48: J51.5, U25.39
- removed net A49: J51.6, U25.38
- removed net A50: J51.7, U25.37
- removed net A51: J51.8, U25.36
- removed net A52: J55.5, U27.39
- removed net A53: J55.6, U27.38
- removed net A54: J55.7, U27.37
- removed net A55: J55.8, U27.36
- removed net A56: J59.5, U29.39
- removed net A57: J59.6, U29.38
- removed net A58: J59.7, U29.37
- removed net A59: J59.8, U29.36
- removed net A8: J11.5, U5.39
- removed net A9: J11.6, U5.38
- removed net AREF12: C111.2, U25.42
- removed net AREF13: C120.2, U27.42
- removed net AREF14: C129.2, U29.42
- removed net AREF2: C21.2, U5.42
- removed net AREF3: C30.2, U7.42
- removed net AREF4: C39.2, U9.42
- removed net AREF7: C66.2, U15.42
- removed net AREF8: C75.2, U17.42
- removed net AREF9: C84.2, U19.42
- removed net D+12: R128.2, U25.4
- removed net D+13: R138.2, U27.4
- removed net D+14: R148.2, U29.4
- removed net D+2: R28.2, U5.4
- removed net D+3: R38.2, U7.4
- removed net D+4: R48.2, U9.4
- removed net D+7: R78.2, U15.4
- removed net D+8: R88.2, U17.4
- removed net D+9: R98.2, U19.4
- removed net D-12: R127.2, U25.3
- removed net D-13: R137.2, U27.3
- removed net D-14: R147.2, U29.3
- removed net D-2: R27.2, U5.3
- removed net D-3: R37.2, U7.3
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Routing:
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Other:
- board size 104.6 x 128.3 mm -> 103.6 x 148.6 mm
- board text added: "route out"
- board text added: "vscore"
- board text removed: "Route Out"
- board text removed: "v-score"
